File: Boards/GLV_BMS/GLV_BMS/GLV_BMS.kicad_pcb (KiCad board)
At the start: 2 copper layers, 91.4 x 66 mm, 44 parts, among them J1 CONN_02X03, J2 CONN_02X03, J3 MM_F_RA_20, U1 MCP2561-E_SN, U101 TPS560430YF, U2 ATMEGA16M1, U3 ATmega328P-AU, Y1 Crystal_SMD, Y2 Crystal_SMD

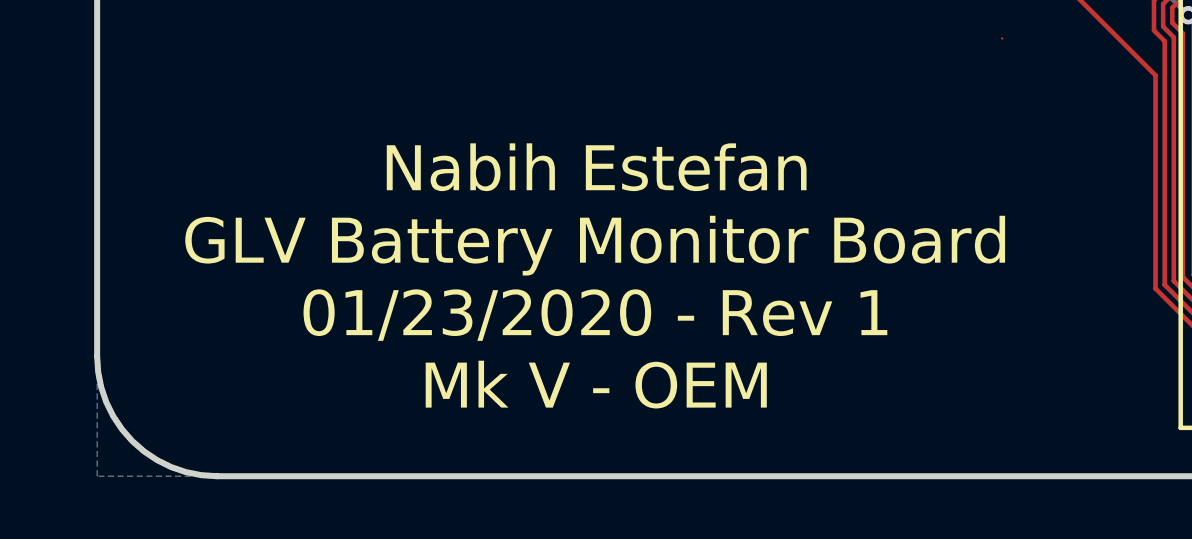
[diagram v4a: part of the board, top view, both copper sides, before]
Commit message: Turned pins for repositioning. Finished Rev 2
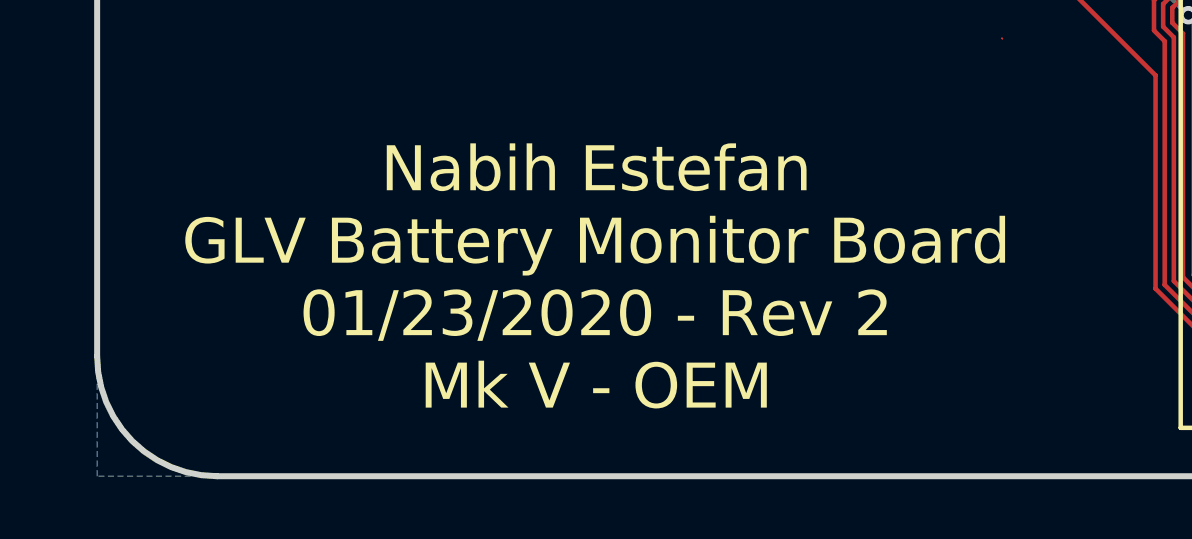
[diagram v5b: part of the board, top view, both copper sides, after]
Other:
- board text added: "Nabih Estefan GLV Battery Monitor Board 01/23/2020 - Rev 2 Mk V - OEM"
- board text removed: "Nabih Estefan GLV Battery Monitor Board 01/23/2020 - Rev 1 Mk V - OEM"
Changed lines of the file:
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@@
     (effects (font (size 1.5 1.5) (thickness 0.3)))
   )
-  (gr_text "Nabih Estefan\nGLV Battery Monitor Board\n01/23/2020 - Rev 1\nMk V - OEM\n" (at 115.697 129.286) (layer F.SilkS)
+  (gr_text "Nabih Estefan\nGLV Battery Monitor Board\n01/23/2020 - Rev 2\nMk V - OEM\n" (at 115.697 129.286) (layer F.SilkS)
     (effects (font (size 1.5 1.5) (thickness 0.3)))
   )

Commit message: Board finished, pushing Rev 2
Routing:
- net VCC: track 179.6 -> 177.6 mm
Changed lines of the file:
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@@
     (thickness 1.6)
     (drawings 52)
-    (tracks 728)
+    (tracks 726)
     (zones 0)
     (modules 44)
@@
   )
   (setup
-    (last_trace_width 0.254)
+    (last_trace_width 0.1524)
     (user_trace_width 0.254)
     (user_trace_width 0.381)
@@
   (segment (start 171.80982 101.1128) (end 170.5377 101.1128) (width 0.254) (layer F.Cu) (net 2))
   (segment (start 170.5377 101.1128) (end 169.9337 101.1128) (width 0.254) (layer F.Cu) (net 2))
-  (segment (start 172.72762 98.56) (end 164.8087 90.64108) (width 0.381) (layer F.Cu) (net 2))
-  (segment (start 172.72762 99.441) (end 172.72762 98.56) (width 0.381) (layer F.Cu) (net 2))
-  (segment (start 164.8087 90.64108) (end 163.42242 90.64108) (width 0.381) (layer F.Cu) (net 2))
-  (segment (start 163.42242 90.64108) (end 161.3027 92.7608) (width 0.381) (layer F.Cu) (net 2))
   (segment (start 144.4084 112.1664) (end 144.4244 112.1504) (width 0.254) (layer F.Cu) (net 2))
   (segment (start 142.1384 112.1664) (end 144.4084 112.1664) (width 0.254) (layer F.Cu) (net 2))
@@
   (segment (start 151.8158 92.964) (end 151.7904 92.9386) (width 0.254) (layer F.Cu) (net 2))
   (segment (start 154.813 92.964) (end 151.8158 92.964) (width 0.254) (layer F.Cu) (net 2))
-  (segment (start 161.3027 92.7608) (end 161.0995 92.964) (width 0.254) (layer F.Cu) (net 2))
   (segment (start 158.877 92.964) (end 158.623 92.964) (width 0.254) (layer F.Cu) (net 2))
   (segment (start 158.877 92.964) (end 154.813 92.964) (width 0.254) (layer F.Cu) (net 2))
@@
   (segment (start 150.4696 113.538) (end 147.574004 113.538) (width 0.254) (layer F.Cu) (net 2))
   (segment (start 154.2796 109.728) (end 150.4696 113.538) (width 0.254) (layer F.Cu) (net 2))
+  (segment (start 167.13162 92.964) (end 161.0995 92.964) (width 0.381) (layer F.Cu) (net 2))
+  (segment (start 172.72762 99.441) (end 172.72762 98.56) (width 0.381) (layer F.Cu) (net 2))
+  (segment (start 172.72762 98.56) (end 167.13162 92.964) (width 0.381) (layer F.Cu) (net 2))
   (segment (start 140.2654 112.1394) (end 140.2384 112.1664) (width 0.1524) (layer F.Cu) (net 3))
   (segment (start 140.2654 110.1344) (end 140.2654 112.1394) (width 0.1524) (layer F.Cu) (net 3))
@@
   (segment (start 116.408495 99.520595) (end 119.060588 99.520595) (width 0.1524) (layer F.Cu) (net 7))
   (segment (start 114.5286 96.8883) (end 114.5286 97.6407) (width 0.1524) (layer F.Cu) (net 7))
-  (segment (start 179.39502 97.16516) (end 179.39502 98.84928) (width 0.254) (layer F.Cu) (net 8))
   (segment (start 179.2732 101.1351) (end 179.2679 101.1404) (width 0.254) (layer F.Cu) (net 8))
   (segment (start 179.2679 101.1404) (end 179.2679 102.0904) (width 0.381) (layer F.Cu) (net 8))
-  (segment (start 179.39502 98.84928) (end 179.2732 98.9711) (width 0.254) (layer F.Cu) (net 8))
   (segment (start 179.2732 98.9711) (end 179.2732 101.1351) (width 0.254) (layer F.Cu) (net 8))
   (segment (start 179.1357 98.8336) (end 179.2732 98.9711) (width 0.254) (layer F.Cu) (net 8))
   (segment (start 176.6062 98.8336) (end 179.1357 98.8336) (width 0.254) (layer F.Cu) (net 8))
-  (segment (start 179.39502 89.02412) (end 179.39502 96.59016) (width 0.254) (layer F.Cu) (net 8))
-  (segment (start 179.39502 96.59016) (end 179.39502 97.16516) (width 0.254) (layer F.Cu) (net 8))
   (segment (start 177.9397 87.5688) (end 177.9957 87.6248) (width 0.254) (layer F.Cu) (net 8))
   (segment (start 177.9837 87.6128) (end 177.9957 87.6248) (width 0.254) (layer F.Cu) (net 8))
   (segment (start 177.9397 87.2998) (end 177.9397 87.5688) (width 0.254) (layer F.Cu) (net 8))
-  (segment (start 177.9957 87.6248) (end 179.39502 89.02412) (width 0.254) (layer F.Cu) (net 8))
+  (segment (start 179.39502 98.84928) (end 179.2732 98.9711) (width 0.254) (layer F.Cu) (net 8))
+  (segment (start 179.39502 95.57502) (end 179.39502 98.84928) (width 0.254) (layer F.Cu) (net 8))
+  (segment (start 177.9957 87.6248) (end 178.054 87.6831) (width 0.254) (layer F.Cu) (net 8))
+  (segment (start 178.054 94.234) (end 179.39502 95.57502) (width 0.254) (layer F.Cu) (net 8))
+  (segment (start 178.054 87.6831) (end 178.054 94.234) (width 0.254) (layer F.Cu) (net 8))
   (segment (start 179.0188 103.2895) (end 179.2679 103.0404) (width 0.254) (layer F.Cu) (net 9))
   (segment (start 179.2679 105.2998) (end 179.3527 105.3846) (width 0.254) (layer F.Cu) (net 9))
@@
   )
   (zone (net 1) (net_name GND) (layer B.Cu) (hatch edge 0.508)
-    (connect_pads (clearance 0.1524))
+    (connect_pads yes (clearance 0.1524))
     (min_thickness 0.254)
     (fill yes (arc_segments 32) (thermal_gap 0.508) (thermal_bridge_width 0.508))

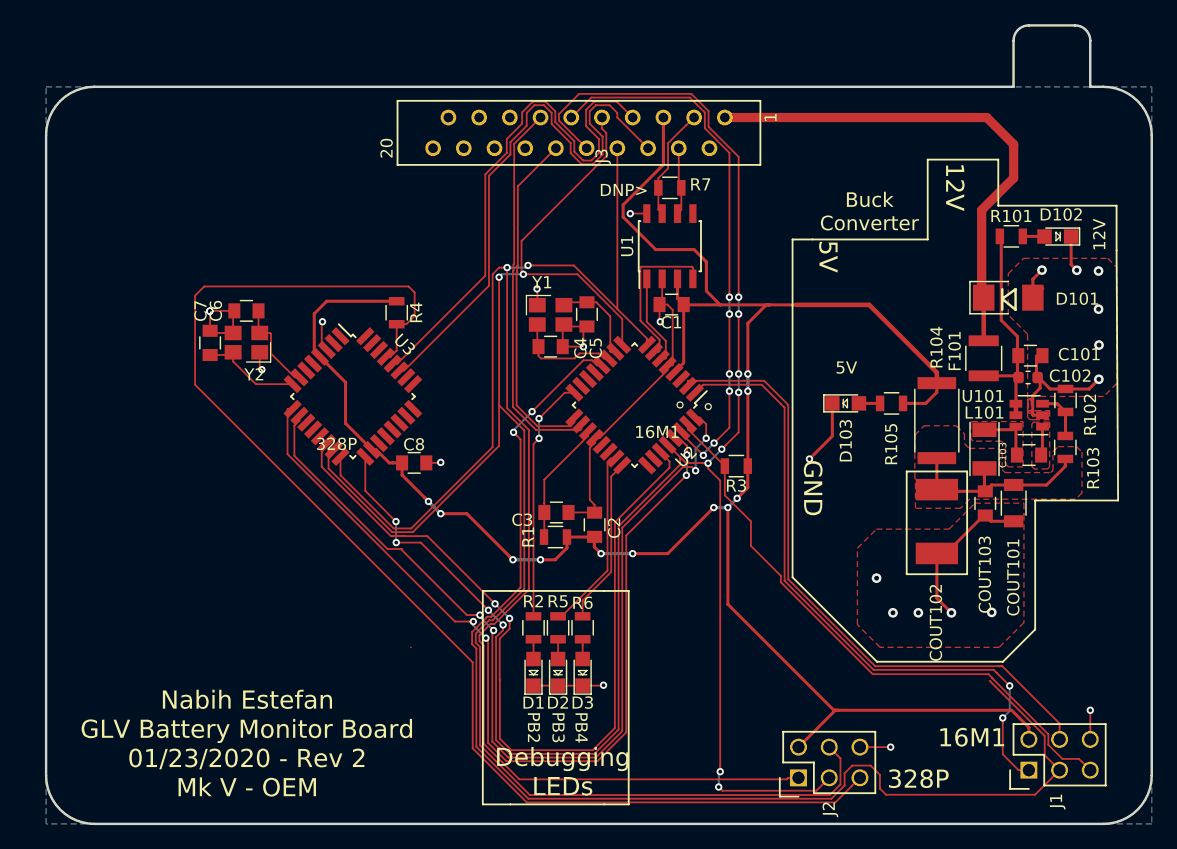
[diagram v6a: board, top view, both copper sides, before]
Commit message: Rev 3, reduced number of vias and was able to reorganize some tracks
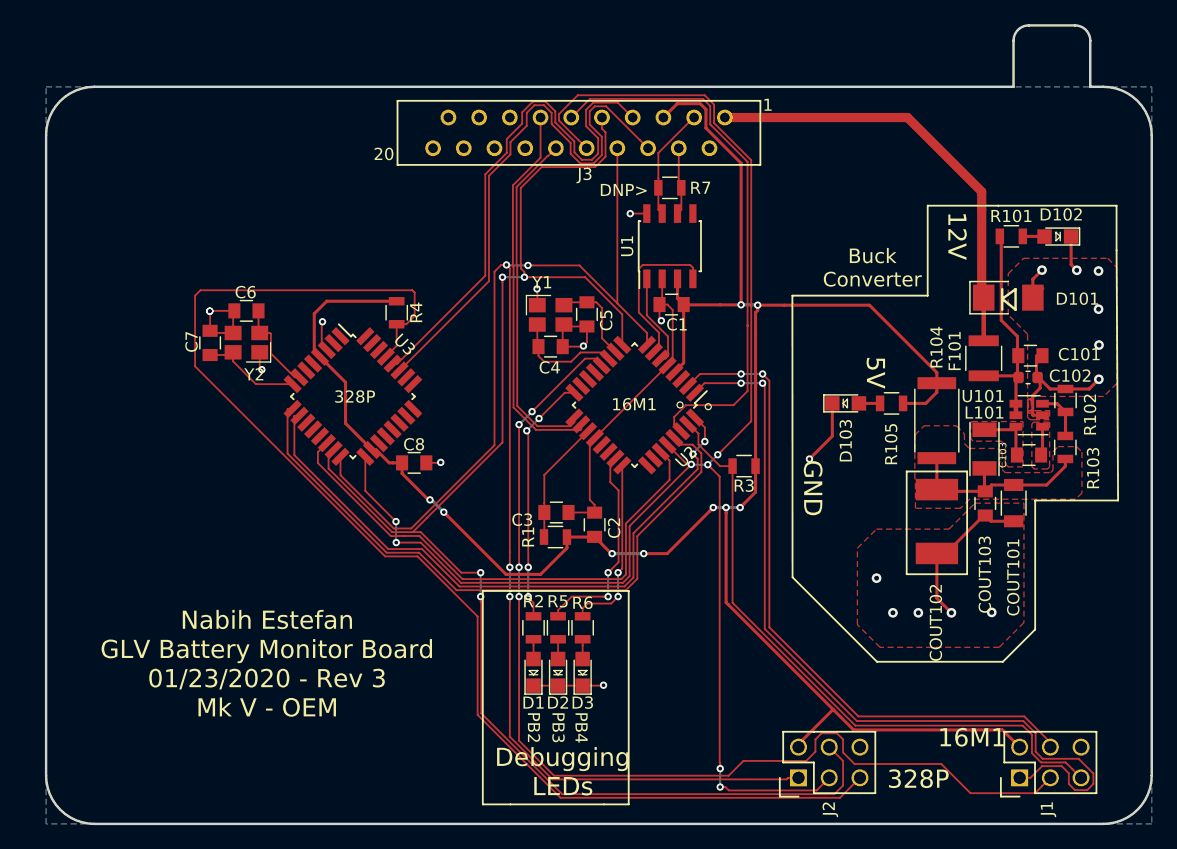
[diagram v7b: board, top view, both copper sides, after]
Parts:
- moved J1 0.99 mm to (179.6, 132.1)
- moved R3 0.64 mm to (156.8, 106.3)
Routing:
- net /CS_2: track 70.2 -> 43.7 mm, vias 2 -> 0
- net /INFO2: track 78.2 -> 53.5 mm, vias 4 -> 2
- net /SCK_2: track 155.2 -> 131.2 mm, vias 12 -> 7
- net /INFO1: track 75.9 -> 53.4 mm, vias 4 -> 0
- net /SCK: track 102.3 -> 85.9 mm, vias 2 -> 4
- net /MISO: track 53.6 -> 68.3 mm
- net /MOSI_2: track 131.5 -> 122.9 mm, vias 2 -> 4
- net +12V: track 42.3 -> 36.3 mm
- net GND: track 98.4 -> 92.9 mm, vias 24 -> 22
- net /MISO_2: track 131.9 -> 126.8 mm, vias 2 -> 4
- net /RESET: track 48.9 -> 52.4 mm
- net /MOSI: track 52.7 -> 55.3 mm, vias 0 -> 2
- net /LED_2: track 15.4 -> 17.6 mm, vias 0 -> 2
- net VCC: track 177.6 -> 176.5 mm, vias 11 -> 9
- net /LED_3: track 13.8 -> 15.0 mm, vias 0 -> 2
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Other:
- board text added: "Nabih Estefan GLV Battery Monitor Board 01/23/2020 - Rev 3 Mk V - OEM"
- board text removed: "Nabih Estefan GLV Battery Monitor Board 01/23/2020 - Rev 2 Mk V - OEM"
